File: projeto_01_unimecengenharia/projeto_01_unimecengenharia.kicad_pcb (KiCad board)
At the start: 2 copper layers, 2 parts, among them U1 ESP32-WROOM-32D, U2 SIM7080G

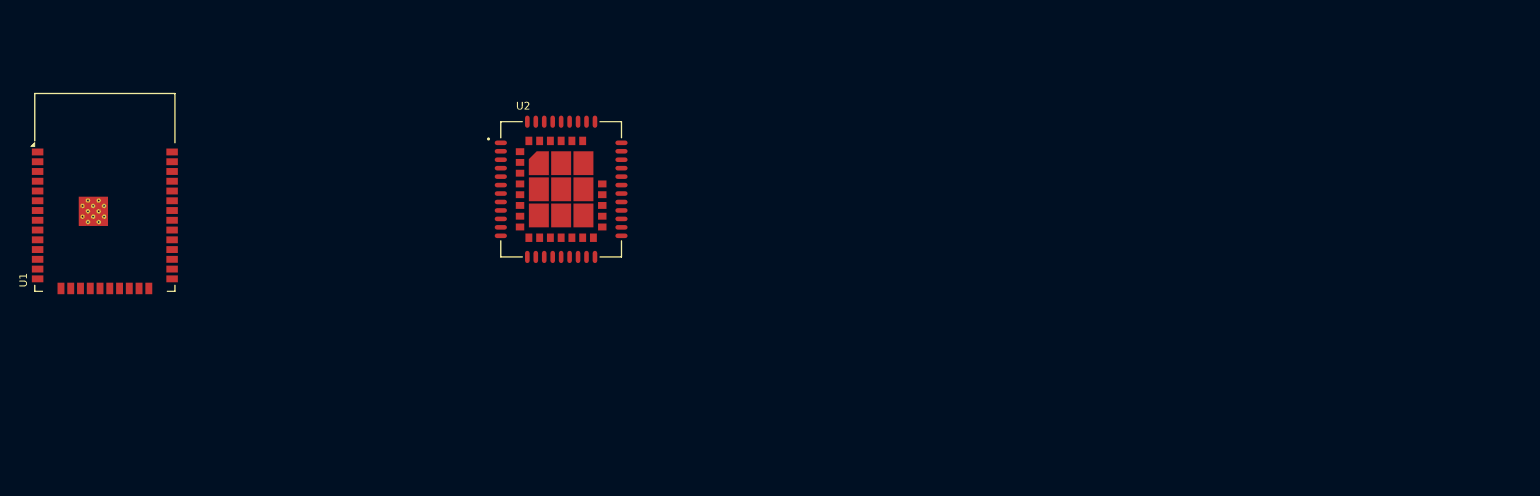
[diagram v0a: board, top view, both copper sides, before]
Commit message: criei a pcb em retangulo
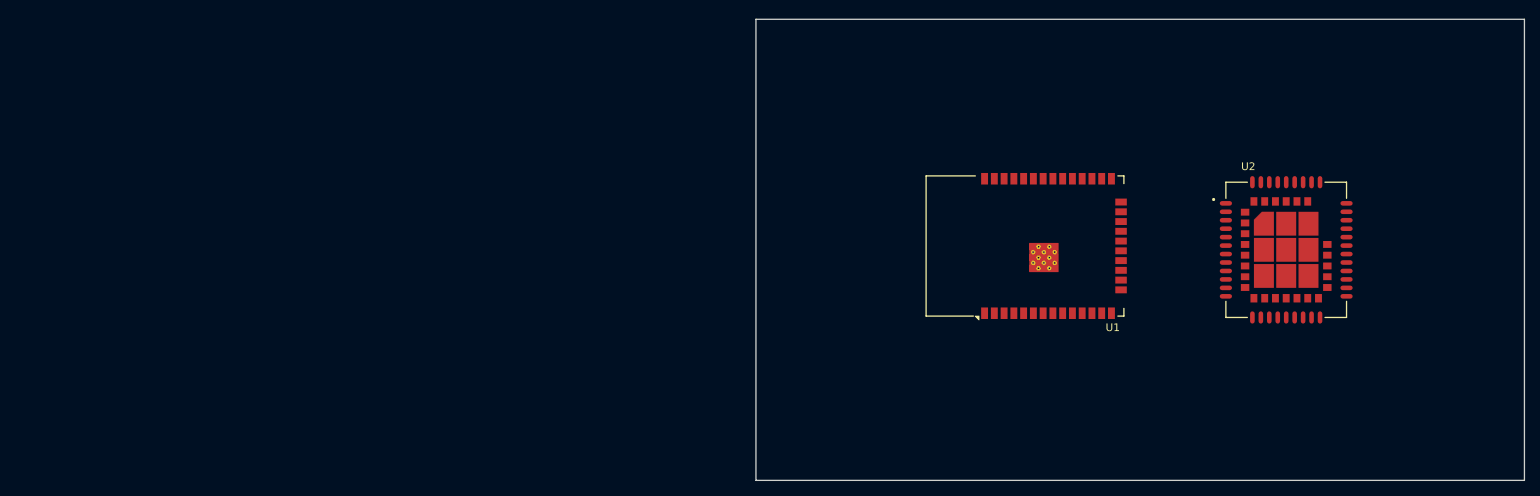
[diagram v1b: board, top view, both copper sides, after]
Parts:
- moved U1 122.8 mm to (184.0, 70.0), turned to 90 degrees
- moved U2 94.7 mm to (215.0, 70.5)
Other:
- board outline added: 100 x 60 mm

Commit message: coloquei mais componentes
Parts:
- added U3: ADS1115IDGS, Package_SO:TSSOP-10_3x3mm_P0.5mm, F.Cu at (203.2, 91.3)
- added U4: DS3231MZ, Package_SO:SOIC-8_3.9x4.9mm_P1.27mm, F.Cu at (203.2, 80.4)
- added U5: MAX3485, Package_SO:SOIC-8_3.9x4.9mm_P1.27mm, F.Cu at (224.7, 91.4)
- added U6: LM2596S-ADJ, Package_TO_SOT_SMD:TO-263-5_TabPin3, F.Cu at (223.7, 47.7)
- moved U1 13.7 mm to (175.5, 80.7), turned to 0 degrees
- moved U2 10.5 mm to (225.5, 71.0)

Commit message: iniciei as ligações dos componentes
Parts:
- removed U6: LM2596S-ADJ, Package_TO_SOT_SMD:TO-263-5_TabPin3
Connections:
- U1 pad 10: unconnected-(U1-IO25-Pad10) -> Net-(U1-IO25)
- U1 pad 12: unconnected-(U1-IO27-Pad12) -> Net-(U1-IO27)
- U1 pad 26: unconnected-(U1-IO4-Pad26) -> Net-(U1-IO4)
- U1 pad 27: unconnected-(U1-IO16-Pad27) -> Net-(U1-IO16)
- U1 pad 28: unconnected-(U1-IO17-Pad28) -> Net-(U1-IO17)
- U1 pad 33: unconnected-(U1-IO21-Pad33) -> Net-(U1-IO21)
- U1 pad 36: unconnected-(U1-IO22-Pad36) -> Net-(U1-IO22)
- U1 pad 4: unconnected-(U1-SENSOR_VP-Pad4) -> Net-(U1-SENSOR_VP)
- U1 pad 5: unconnected-(U1-SENSOR_VN-Pad5) -> Net-(U1-SENSOR_VN)
- U1 pad 6: unconnected-(U1-IO34-Pad6) -> Net-(U1-IO34)
- U1 pad 7: unconnected-(U1-IO35-Pad7) -> Net-(U1-IO35)
- U1 pad 8: unconnected-(U1-IO32-Pad8) -> Net-(U1-IO32)
- U1 pad 9: unconnected-(U1-IO33-Pad9) -> Net-(U1-IO33)
- U2 pad 1: unconnected-(U2-UART1_TXD-Pad1) -> Net-(U1-IO33)
- U2 pad 2: unconnected-(U2-UART1_RXD-Pad2) -> Net-(U1-IO32)
- U2 pad 3: unconnected-(U2-UART1_RTS-Pad3) -> Net-(U1-IO25)
- U2 pad 39: unconnected-(U2-PWRKEY-Pad39) -> Net-(U1-IO27)
- U2 pad 4: unconnected-(U2-UART1_CTS-Pad4) -> Net-(U1-SENSOR_VP)
- U2 pad 42: unconnected-(U2-STATUS-Pad42) -> Net-(U1-IO34)
- U3 pad 10: unconnected-(U3-SCL-Pad10) -> Net-(U1-IO22)
- U3 pad 2: unconnected-(U3-ALERT/RDY-Pad2) -> Net-(U1-IO35)
- U3 pad 9: unconnected-(U3-SDA-Pad9) -> Net-(U1-IO21)
- U4 pad 3: unconnected-(U4-~{INT}/SQW-Pad3) -> Net-(U1-SENSOR_VN)
- U4 pad 7: unconnected-(U4-SDA-Pad7) -> Net-(U1-IO21)
- U4 pad 8: unconnected-(U4-SCL-Pad8) -> Net-(U1-IO22)
- U5 pad 1: unconnected-(U5-RO-Pad1) -> Net-(U1-IO16)
- U5 pad 2: unconnected-(U5-~{RE}-Pad2) -> Net-(U1-IO4)
- U5 pad 3: unconnected-(U5-DE-Pad3) -> Net-(U1-IO4)
- U5 pad 4: unconnected-(U5-DI-Pad4) -> Net-(U1-IO17)
